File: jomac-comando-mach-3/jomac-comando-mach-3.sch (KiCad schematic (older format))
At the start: 80 parts, among them Q1 Q_NPN_CBE, Q10 Q_PNP_CBE, Q2 C, Q3 Q_NPN_CBE, Q4 Q_NPN_CBE, Q5 Q_NPN_CBE, Q6 Q_NPN_CBE, Q7 Q_NPN_CBE, Q8 Q_NPN_CBE, Q9 Q_NPN_CBE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

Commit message: Tweak schematics
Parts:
- gave numbers to parts that had none: 2
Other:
- moved on the sheet: BT1, C1, C10, C12, C19, C2, C3, C4, C5, C6, C7, C8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

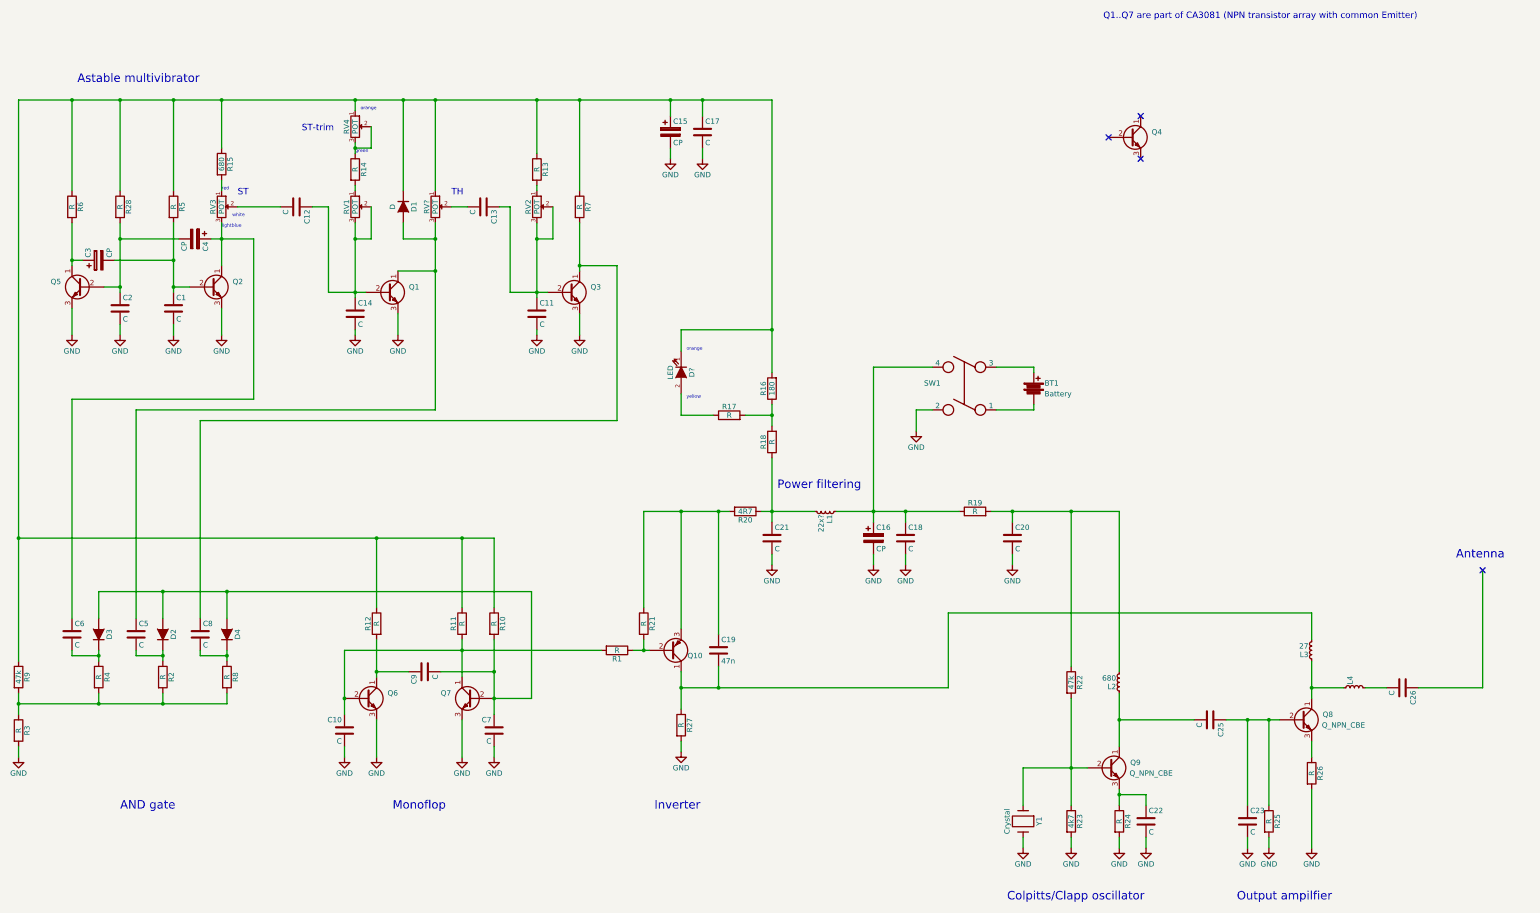
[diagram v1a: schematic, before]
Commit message: Add component values
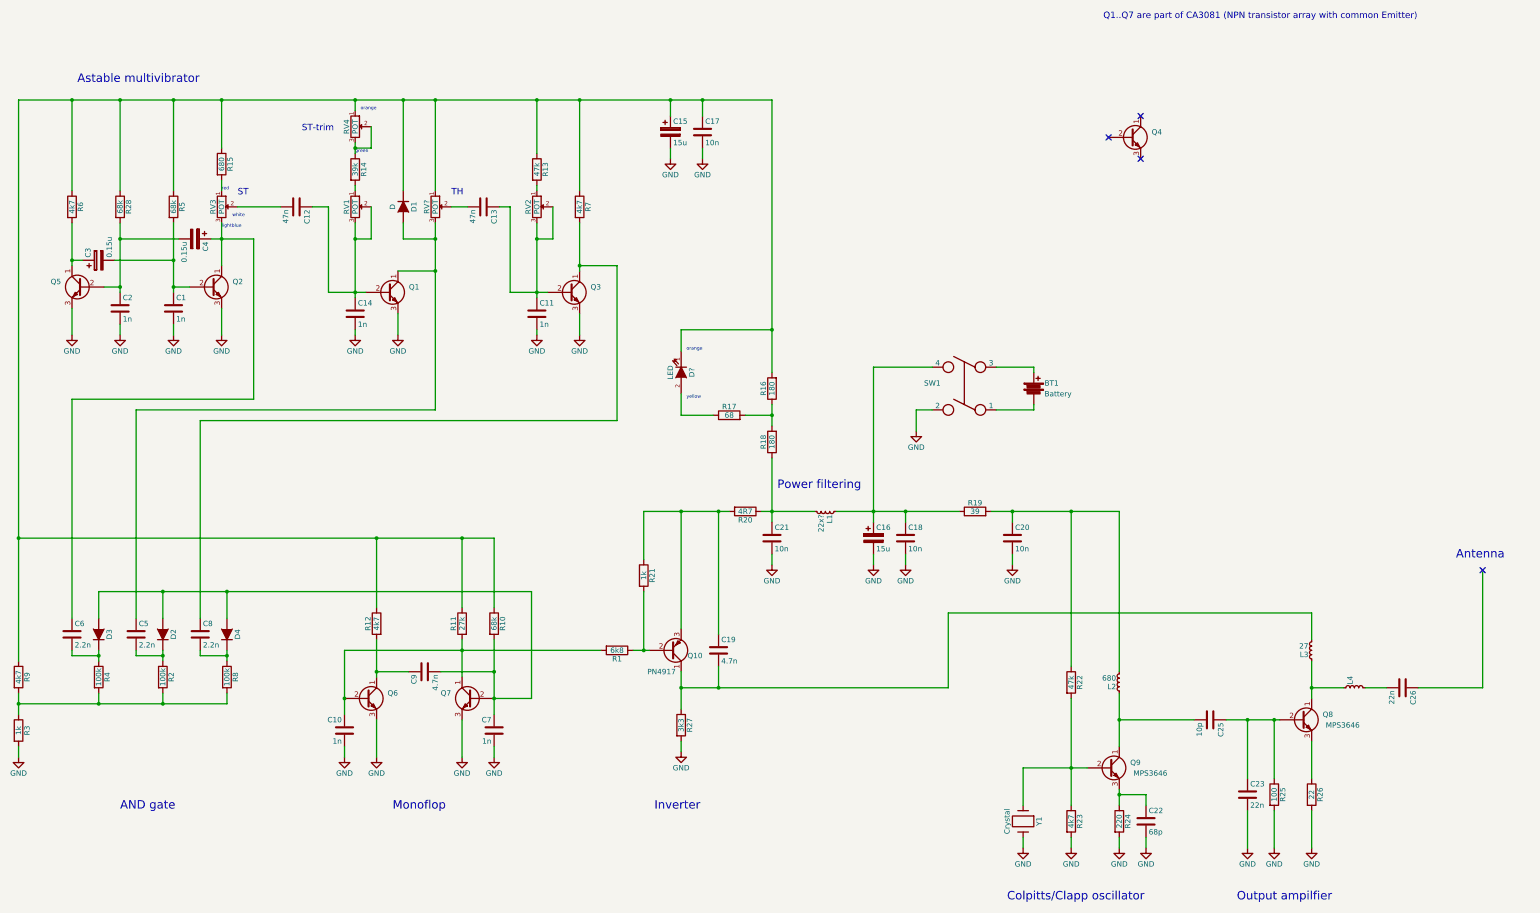
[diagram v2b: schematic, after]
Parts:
- C1, C10, C11, C14, C2, C7: value C -> 1n
- C12, C13: value C -> 47n
- C15, C16: value CP -> 15u
- C17, C18, C20, C21: value C -> 10n
- C19: value 47n -> 4.7n
- C22: value C -> 68p
- C23, C26: value C -> 22n
- C25: value C -> 10p
- C3, C4: value CP -> 0.15u
- C5, C6, C8: value C -> 2.2n
- C9: value C -> 4.7n
- Q10: value Q_PNP_CBE -> PN4917
- Q8, Q9: value Q_NPN_CBE -> MPS3646
- R1: value R -> 6k8
- R10, R28, R5: value R -> 68k
- R11: value R -> 27k
- R12, R6, R7: value R -> 4k7
- R13: value R -> 47k
- R14: value R -> 39k
- R17: value R -> 68
- R18: value R -> 180
- R19: value R -> 39
- R2, R4, R8: value R -> 100k
- R21, R3: value R -> 1k
- R24: value R -> 220
- R25: value R -> 100
- R26: value R -> 22
- R27: value R -> 3k3
- R9: value 47k -> 4k7
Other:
- moved on the sheet: C23, R21, R25, R26
